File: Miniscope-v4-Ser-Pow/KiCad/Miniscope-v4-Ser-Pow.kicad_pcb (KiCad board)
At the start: 6 copper layers, 35 parts, among them J16 Conn_01x20_Female, U1 DS90UB933-Q1, U3 TLV7103318DSER

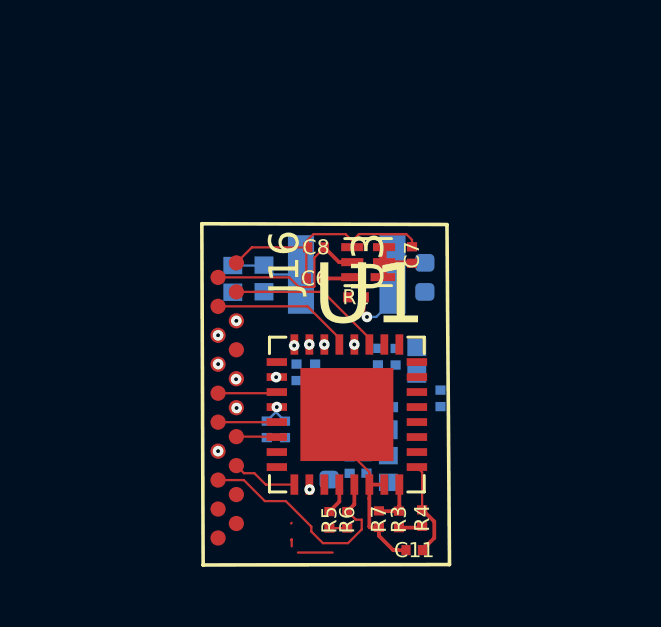
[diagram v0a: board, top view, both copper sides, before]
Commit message: Size update
Things added:

- New coax connector (U.FL-R-SMT-1 from Hirose)
- New pad at the bottom for extra connections
- Power planes

To do:

- Check serializer footprint
- Correct track sizes
- Check via drill sizes
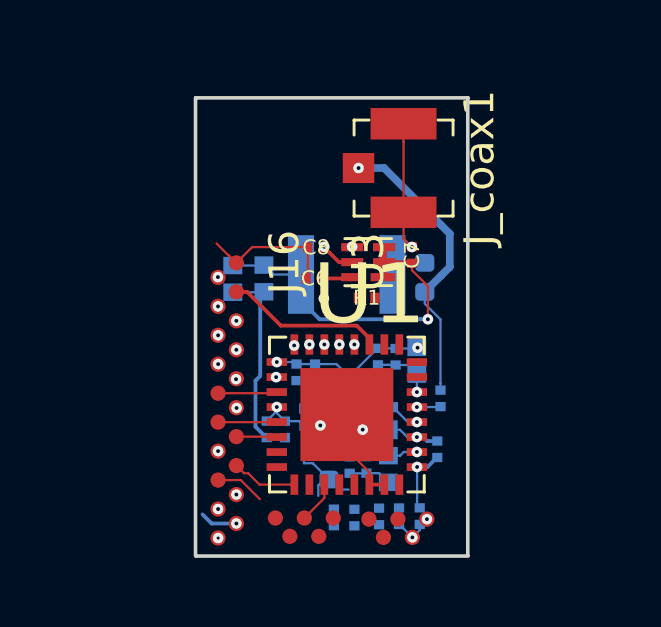
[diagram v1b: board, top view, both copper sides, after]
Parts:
- added J_coax1: U_FL-R-SMT_10_, digikey-footprints:Coax_Conn_U.FL, F.Cu at (121.1, 39.5)
- added J_extra1: Conn_01x05, .Connector:B2B_Flex_05_Dual_Row_38milx24mil_Pad_20mil, F.Cu at (116.9, 51.2)
- added J_extra2: Conn_01x05, .Connector:B2B_Flex_05_Dual_Row_38milx24mil_Pad_20mil, F.Cu at (120.0, 51.2)
- C11, R3, R4, R5, R6, R7: moved to B.Cu
- moved R4 2.35 mm to (122.3, 48.9), turned to 270 degrees
- moved C11 1.15 mm to (121.7, 51.1), turned to 270 degrees
- moved R7 0.68 mm to (121.0, 51.1)
- moved R3 0.67 mm to (120.3, 51.1)
- moved R1 0.36 mm to (119.9, 43.8), turned to 180 degrees
- moved R6 0.25 mm to (119.5, 51.1)
- moved C19 0.22 mm to (118.1, 48.1)
- moved C20 0.22 mm to (118.1, 47.5)
- moved R5 0.17 mm to (118.8, 51.1)
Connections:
- U1 pad 31: (no net) -> DIN10
- U1 pad 32: (no net) -> DIN11
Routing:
- net GND: track 17.6 -> 31.8 mm, vias 0 -> 7
- net +5V: track 4.37 -> 16.5 mm, vias 0 -> 2
- net DOUT_P: track 0.00 -> 9.72 mm, vias 0 -> 1
- net CLK_OUT: track 0.00 -> 6.74 mm, vias 0 -> 1
- net +3V3: track 1.60 -> 7.92 mm, vias 0 -> 1
- net I2C_SDA: track 8.06 -> 1.86 mm
- net VDDD: track 7.94 -> 13.3 mm, vias 1 -> 7
- net VDDPLL: track 0.00 -> 3.08 mm, vias 0 -> 1
- net VDDCML: track 0.00 -> 2.77 mm, vias 0 -> 1
- net MODE: track 1.56 -> 0.00 mm
- net Net-(L1-Pad1): track 2.64 -> 1.24 mm, vias 1 -> 0
- net Net-(C10-Pad2): track 0.00 -> 1.00 mm, vias 0 -> 1
- net PDB: track 3.18 -> 2.20 mm, vias 0 -> 1
- net Net-(C9-Pad2): track 0.00 -> 0.79 mm, vias 0 -> 1
- net I2C_SCL: track 1.13 -> 0.46 mm, vias 0 -> 1
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- added copper zone on GND, net GND
- added copper zone on VDDD, net VDDD
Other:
- board outline added: 9.1 x 15.3 mm

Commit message: New size
Moved around the coax connection to make the board shorter
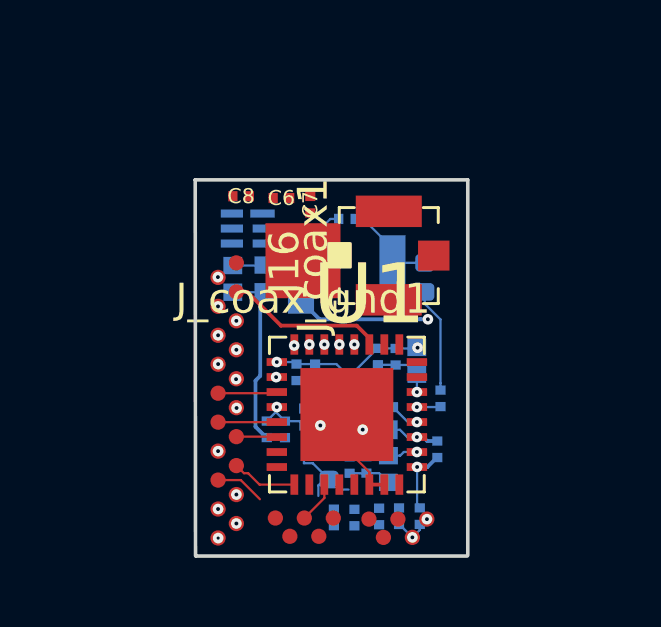
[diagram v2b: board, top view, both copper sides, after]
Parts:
- added J_coax_gnd1: Conn_01x01, .Connector:Conn_1x1_100x100_Pad, F.Cu at (117.8, 42.6)
- R1, U3: moved to B.Cu
- moved U3 4.17 mm to (116.0, 41.5), turned to 270 degrees
- moved C7 3.78 mm to (118.0, 40.7)
- moved C8 3.02 mm to (115.7, 40.4)
- moved J_coax1 2.96 mm to (120.7, 42.4), turned to 90 degrees
- moved C6 2.90 mm to (117.1, 40.5)
- moved R1 2.71 mm to (119.3, 41.2), turned to 0 degrees
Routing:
- net GND: track 31.8 -> 22.7 mm, vias 7 -> 5
- net DOUT_P: track 9.72 -> 3.49 mm, vias 1 -> 0
- net Net-(L1-Pad1): track 1.24 -> 3.76 mm
- net VDDD: track 13.3 -> 10.9 mm, vias 7 -> 6
- net +3V3: track 7.92 -> 6.23 mm, vias 1 -> 0
- net +5V: track 16.5 -> 15.0 mm
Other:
- board size 9.1 x 15.3 mm -> 9.1 x 12.5 mm

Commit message: Almost done
- Everything is connected
- All pads are the same
- Traces are as big as possible

To do

- Final check
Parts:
- C6, C7, C8: moved to B.Cu
- C9: moved to F.Cu
- moved R1 2.37 mm to (120.2, 43.3)
- moved C8 1.87 mm to (115.2, 42.2), turned to 270 degrees
- moved R3 1.61 mm to (121.8, 50.5), turned to 180 degrees
- moved L1 1.56 mm to (119.9, 41.6)
- moved L2 1.39 mm to (122.4, 41.8)
- moved C5 1.36 mm to (116.5, 44.0), turned to 180 degrees
- moved C6 1.18 mm to (115.9, 40.8), turned to 0 degrees
- moved C11 1.16 mm to (121.8, 49.9), turned to 0 degrees
- moved C7 0.98 mm to (117.1, 40.8), turned to 180 degrees
- moved U3 0.74 mm to (116.5, 42.0)
- moved C9 0.53 mm to (122.4, 46.6)
- moved L4 0.48 mm to (118.2, 49.1), turned to 180 degrees
- moved C30 0.47 mm to (117.0, 47.9), turned to 180 degrees
- moved J_coax1 0.41 mm to (120.2, 42.4)
- moved C29 0.35 mm to (117.0, 48.5), turned to 180 degrees
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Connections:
- J16 pad 19: VDDD -> +3V3
- J_extra2 pad 3: +5V -> GND
- J_extra2 pad 4: GND -> +5V
- U1 pad : (no net) -> GND
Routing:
- net +3V3: track 6.23 -> 18.8 mm, vias 0 -> 3
- net +5V: track 15.0 -> 27.0 mm, vias 2 -> 3
- net I2C_SDA: track 1.86 -> 8.97 mm, vias 0 -> 3
- net I2C_SCL: track 0.46 -> 6.72 mm, vias 1 -> 3
- net GND: track 22.7 -> 28.3 mm, vias 5 -> 22
- net DIN10: track 0.00 -> 3.00 mm
- net DIN11: track 0.00 -> 2.49 mm
- net CLK_OUT: track 6.74 -> 9.04 mm, vias 1 -> 2
- net VDDD: track 10.9 -> 9.56 mm
- net MODE: track 0.00 -> 1.34 mm, vias 0 -> 1
- net PDB: track 2.20 -> 1.41 mm
- net DOUT_P: track 3.49 -> 4.20 mm, vias 0 -> 1
- net DIN0: track 5.28 -> 5.86 mm
- net FV: track 3.97 -> 3.81 mm, vias 1 -> 2
- net LV: track 2.20 -> 2.27 mm, vias 0 -> 2
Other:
- board size 9.1 x 12.5 mm -> 9.1 x 12.4 mm

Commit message: Renaming the layers
Renamed the layers to be consistent with the other boards
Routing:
- added copper zone on In1.Cu, net GND
- added copper zone on In3.Cu, net VDDD
- removed copper zone on GND, net GND
- removed copper zone on VDDD, net VDDD

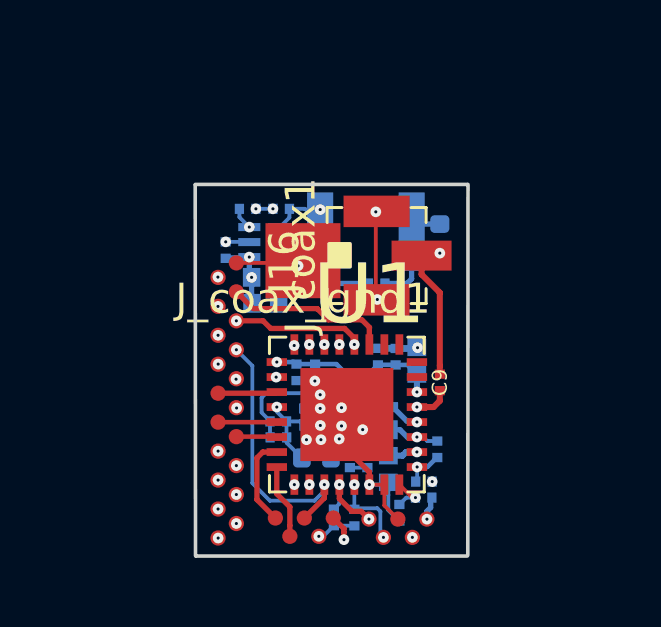
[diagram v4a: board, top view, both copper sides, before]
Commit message: Finalize routing for Ser-Pow PCB
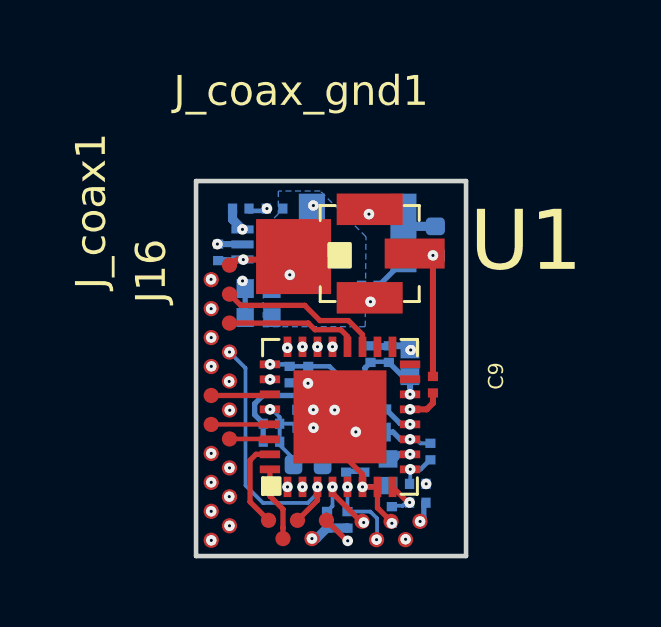
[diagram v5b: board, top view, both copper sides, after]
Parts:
- moved C5 0.53 mm to (116.3, 44.5)
- moved C4 0.43 mm to (116.3, 43.5)
- moved L4 0.36 mm to (118.0, 49.4)
- moved J_coax_gnd1 0.34 mm to (117.5, 42.4)
- moved L1 0.28 mm to (119.6, 41.6)
- moved C29 0.27 mm to (116.7, 48.6)
- moved C8 0.26 mm to (115.0, 42.3)
- moved R7 0.26 mm to (120.8, 51.0)
- moved R3 0.26 mm to (121.6, 50.6)
- moved C27 0.26 mm to (120.0, 45.7)
- moved C28 0.24 mm to (120.7, 45.7)
- moved C10 0.24 mm to (120.3, 47.5)
- moved C18 0.24 mm to (120.0, 48.3)
- moved C19 0.24 mm to (117.9, 48.1)
- moved C21 0.24 mm to (118.0, 46.4)
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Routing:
- net GND: track 28.3 -> 21.8 mm, vias 22 -> 17
- net +5V: track 27.0 -> 24.5 mm
- net I2C_SDA: track 8.97 -> 8.43 mm
- net +3V3: track 18.8 -> 19.3 mm
- net DIN1: track 4.38 -> 4.46 mm, vias 2 -> 0
- added copper zone on B.Cu, net +5V
- added copper zone on In4.Cu, net VDDD
- removed copper zone on In3.Cu, net VDDD
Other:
- board size 9.1 x 12.4 mm -> 9 x 12.5 mm
- net class Default: via_dia 0.8 -> 0.3556; via_drill 0.4 -> 0.1016
- rule pad_to_mask_clearance: 0.051 -> 0.0254
- rule solder_mask_min_width: 0.25 -> 0.1016
- rule via_min_size: 0.254 -> 0.3556
